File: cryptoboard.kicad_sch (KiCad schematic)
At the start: 29 parts, among them J1 USB_A, J2 BOOT, J3 SWD, J4 Conn_01x06, J5 Conn_01x06, SW1 SW_Push, U1 STM32F103C8Tx, U2 LM317_SOT-223-3.3V

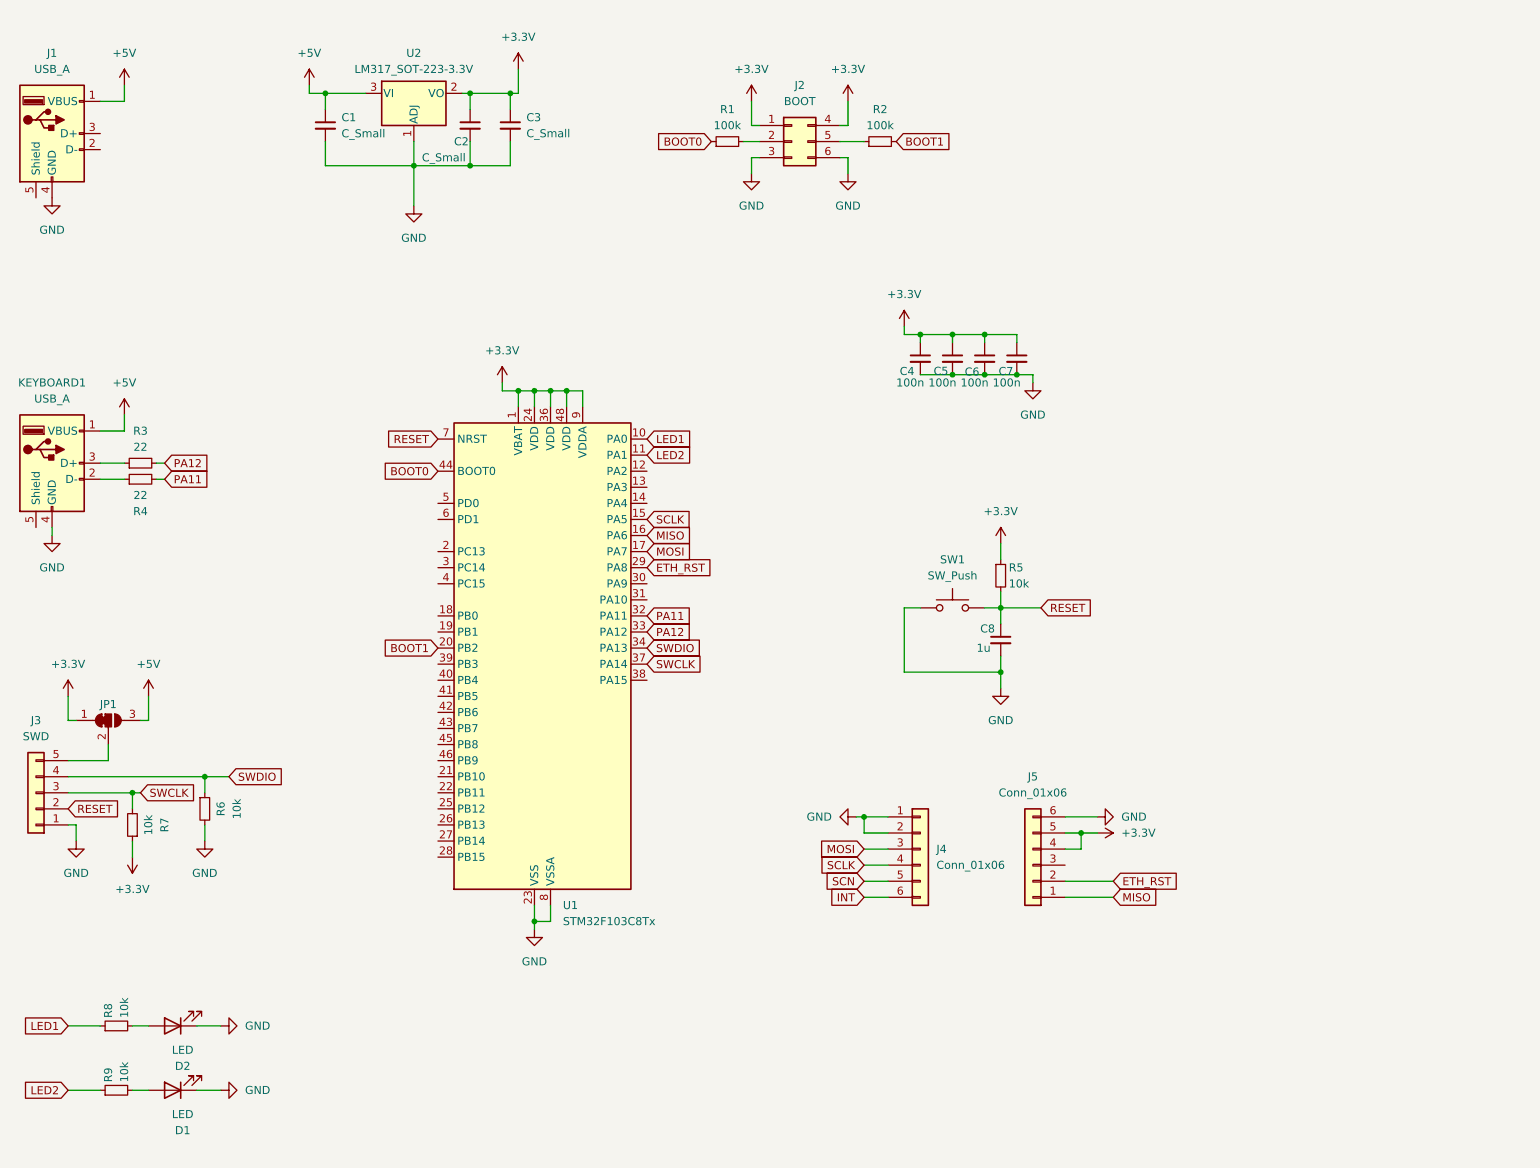
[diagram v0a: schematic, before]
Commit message: add i2c + usr
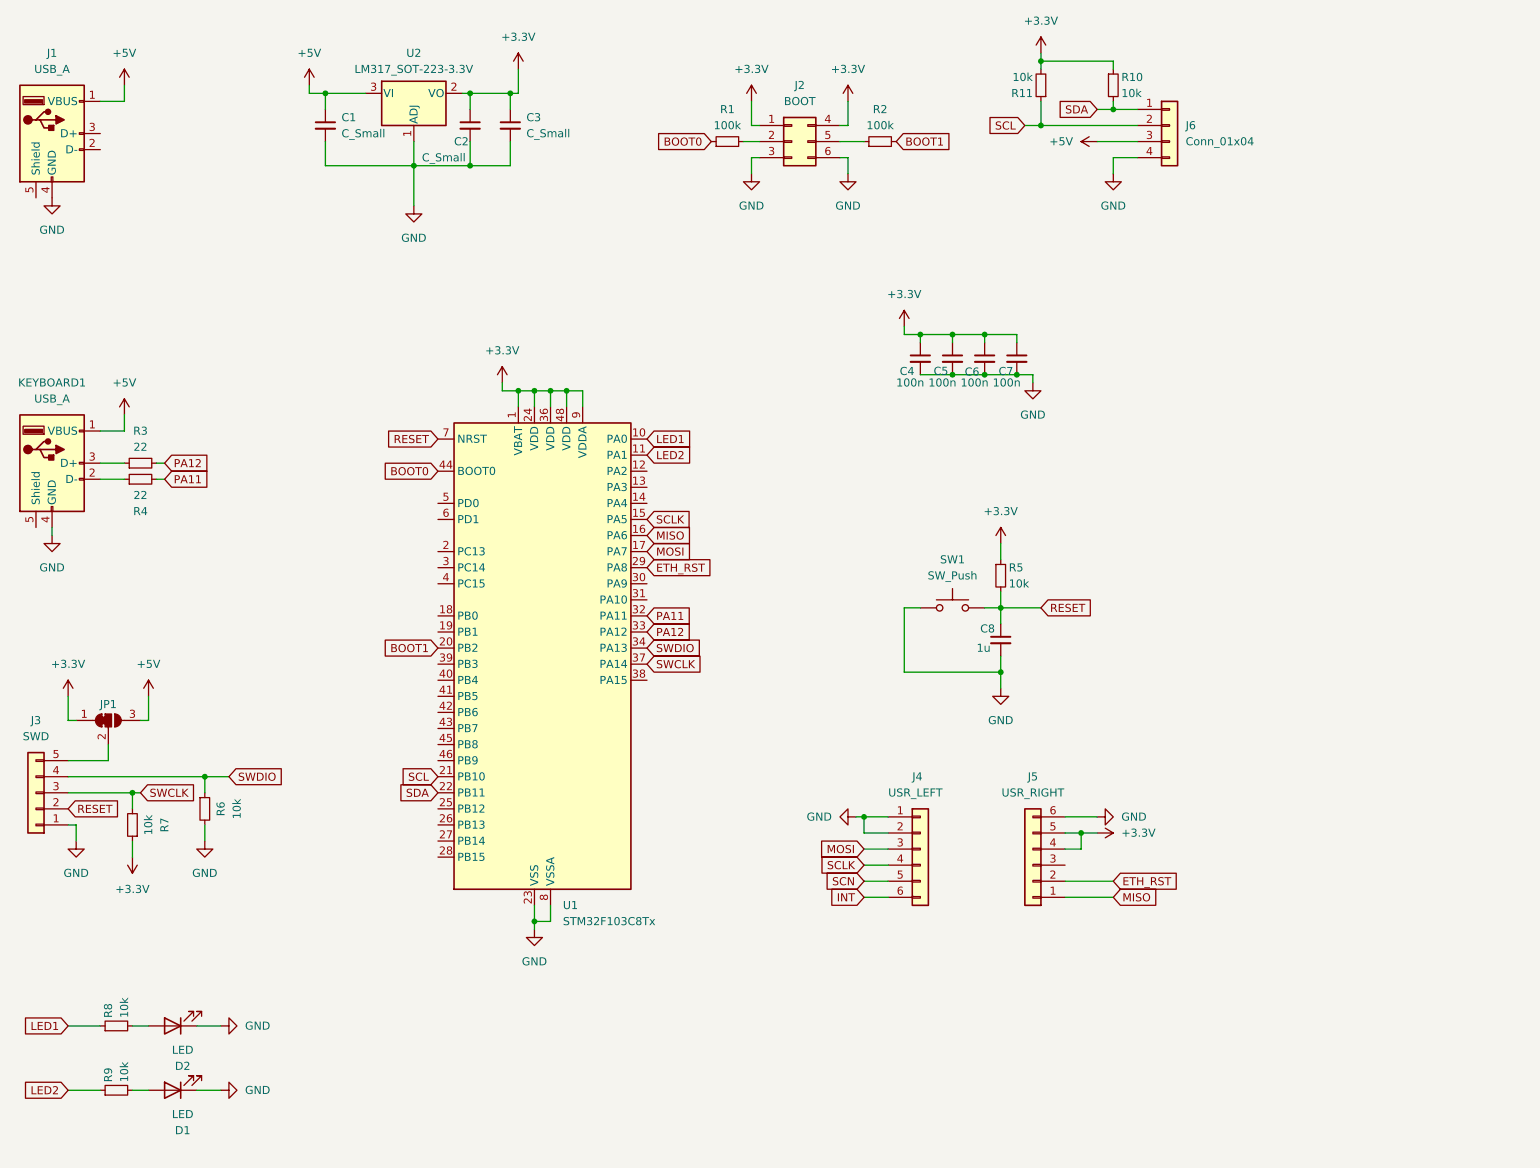
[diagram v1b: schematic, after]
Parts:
- added J6: Conn_01x04, Connector_PinHeader_2.54mm:PinHeader_1x04_P2.54mm_Vertical, symbol Connector_Generic:Conn_01x04
- added R10, R11: 10k, Resistor_SMD:R_0603_1608Metric, symbol Device:R_Small
- J4: value Conn_01x06 -> USR_LEFT; footprint (none) -> Connector_PinHeader_2.54mm:PinHeader_1x06_P2.54mm_Vertical
- J5: value Conn_01x06 -> USR_RIGHT; footprint (none) -> Connector_PinHeader_2.54mm:PinHeader_1x06_P2.54mm_Vertical
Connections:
- net +3.3V: now also R10.1, R11.2
- net +5V: now also J6.3 (Pin_3)
- net GND: now also J6.4 (Pin_4)
- net SCL: now reaches U1.21 (PB10)
- net SCL: now also J6.2 (Pin_2), R11.1
- net SDA: now reaches U1.22 (PB11)
- net SDA: now also J6.1 (Pin_1), R10.2

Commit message: add pcb
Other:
- moved on the sheet: R2
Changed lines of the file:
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@@
+    (stroke (width 0) (type default))
+  )
+  (wire (pts (xy 124.46 33.02) (xy 125.73 33.02))
     (stroke (width 0) (type default))
   )
@@
     (stroke (width 0) (type default))
   )
-  (wire (pts (xy 146.05 33.02) (xy 149.86 33.02))
+  (wire (pts (xy 146.05 33.02) (xy 148.59 33.02))
     (stroke (width 0) (type default))
   )
@@
   )
   (wire (pts (xy 64.77 33.02) (xy 64.77 36.83))
+    (stroke (width 0) (type default))
+  )
+  (wire (pts (xy 154.94 33.02) (xy 153.67 33.02))
     (stroke (width 0) (type default))
   )
@@
     )
   )
-  (global_label "BOOT0" (shape input) (at 125.73 33.02 180) (fields_autoplaced)
+  (global_label "BOOT0" (shape input) (at 124.46 33.02 180) (fields_autoplaced)
     (effects (font (size 1.27 1.27)) (justify right))
-    (property "Intersheetrefs" "${INTERSHEET_REFS}" (at 116.7161 33.02 0)
+    (property "Intersheetrefs" "${INTERSHEET_REFS}" (at 115.4461 33.02 0)
       (effects (font (size 1.27 1.27)) (justify right) hide)
     )
@@
     )
   )
-  (symbol (lib_id "Device:R_Small") (at 152.4 33.02 90) (unit 1)
-    (in_bom yes) (on_board yes) (dnp no) (fields_autoplaced)
-    (property "Reference" "R2" (at 152.4 27.94 90)
-      (effects (font (size 1.27 1.27)))
-    )
-    (property "Value" "100k" (at 152.4 30.48 90)
-      (effects (font (size 1.27 1.27)))
-    )
-    (property "Footprint" "Resistor_SMD:R_0603_1608Metric" (at 152.4 33.02 0)
-      (effects (font (size 1.27 1.27)) hide)
-    )
-    (property "Datasheet" "~" (at 152.4 33.02 0)
-      (effects (font (size 1.27 1.27)) hide)
-    )
+  (symbol (lib_id "Device:R_Small") (at 151.13 33.02 90) (unit 1)
+    (in_bom yes) (on_board yes) (dnp no) (fields_autoplaced)
+    (property "Reference" "R2" (at 151.13 27.94 90)
+      (effects (font (size 1.27 1.27)))
+    )
+    (property "Value" "100k" (at 151.13 30.48 90)
+      (effects (font (size 1.27 1.27)))
+    )
+    (property "Footprint" "Resistor_SMD:R_0603_1608Metric" (at 151.13 33.02 0)
+      (effects (font (size 1.27 1.27)) hide)
+    )
+    (property "Datasheet" "~" (at 151.13 33.02 0)
+      (effects (font (size 1.27 1.27)) hide)
+    )

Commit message: add wiring
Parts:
- J2: footprint Connector_PinHeader_2.54mm:PinHeader_2x03_P2.54mm_Vertical -> Library:PinHeader_2x03_P2.54mm_Vertical_new
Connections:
- net INT: now also U1.18 (PB0)
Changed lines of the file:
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@@
+    )
+  )
+  (global_label "INT" (shape input) (at 82.55 107.95 180) (fields_autoplaced)
+    (effects (font (size 1.27 1.27)) (justify right))
+    (property "Intersheetrefs" "${INTERSHEET_REFS}" (at 76.7413 107.95 0)
+      (effects (font (size 1.27 1.27)) (justify right) hide)
     )
   )
@@
       (effects (font (size 1.27 1.27)))
     )
-    (property "Footprint" "Connector_PinHeader_2.54mm:PinHeader_2x03_P2.54mm_Vertical" (at 138.43 33.02 0)
-      (effects (font (size 1.27 1.27)) hide)
-    )
+    (property "Footprint" "Library:PinHeader_2x03_P2.54mm_Vertical_new" (at 138.43 33.02 0)
+      (effects (font (size 1.27 1.27)) hide)
+    )

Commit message: add crystal
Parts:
- added C10, C9: 20p, Capacitor_SMD:C_0603_1608Metric, symbol Device:C_Small
- added R12: 1M, Resistor_SMD:R_0603_1608Metric, symbol Device:R_Small
- added Y1: Crystal, Crystal:Crystal_SMD_HC49-SD, symbol Device:Crystal
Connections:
- net GND: now also C10.2, C9.2
- net OSIN: now reaches U1.5 (PD0)
- net OSIN: now also C9.1, R12.1, Y1.2
- net OSOUT: now reaches U1.6 (PD1)
- net OSOUT: now also C10.1, R12.2, Y1.1

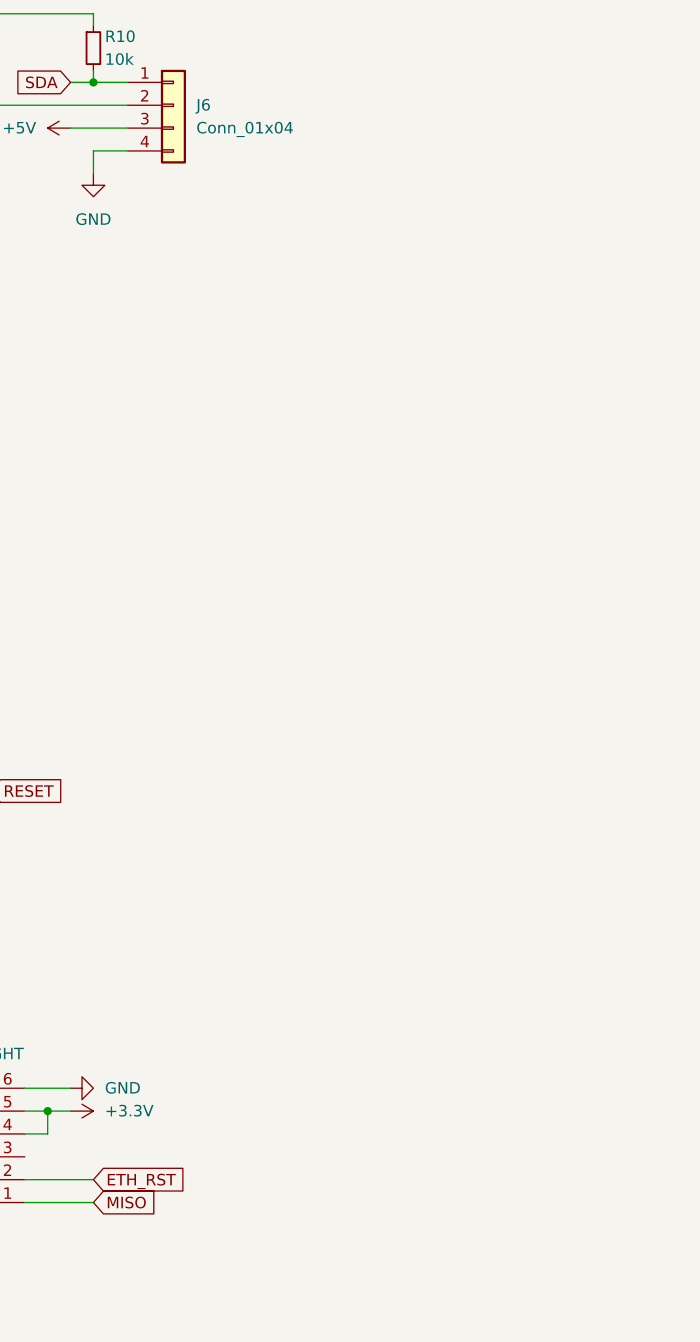
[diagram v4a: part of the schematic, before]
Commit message: stm32f103 to stm32f107
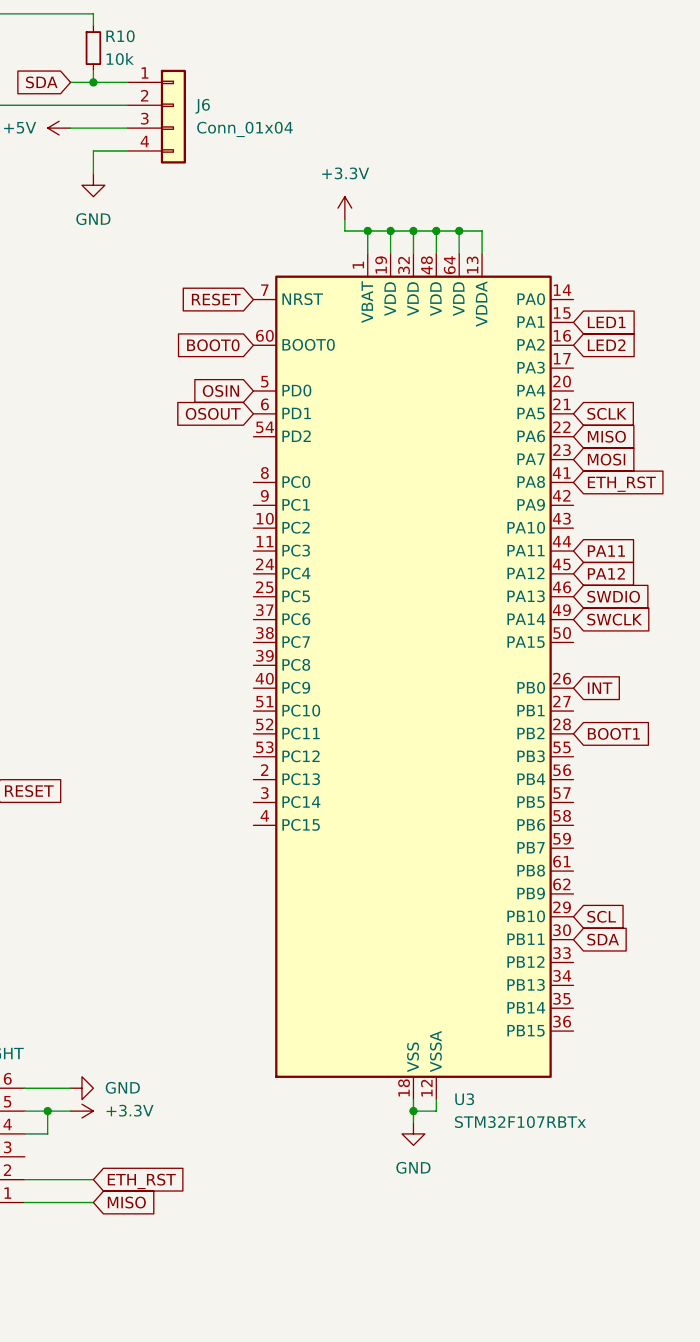
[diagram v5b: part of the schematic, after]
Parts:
- added U3: STM32F107RBTx, Package_QFP:LQFP-64_10x10mm_P0.5mm, symbol MCU_ST_STM32F1:STM32F107RBTx
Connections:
- net +3.3V: now also U3.1 (VBAT), U3.13 (VDDA), U3.19 (VDD), U3.32 (VDD), U3.48 (VDD), U3.64 (VDD)
- net BOOT0: now also U3.60 (BOOT0)
- net BOOT1: now also U3.28 (PB2)
- net ETH_RST: now also U3.41 (PA8)
- net GND: now also U3.12 (VSSA), U3.18 (VSS), U3.31 (VSS), U3.47 (VSS), U3.63 (VSS)
- net INT: now also U3.26 (PB0)
- net LED1: now also U3.15 (PA1)
- net LED2: now also U3.16 (PA2)
- net MISO: now also U3.22 (PA6)
- net MOSI: now also U3.23 (PA7)
- net OSIN: now also U3.5 (PD0)
- net OSOUT: now also U3.6 (PD1)
- net PA11: now also U3.44 (PA11)
- net PA12: now also U3.45 (PA12)
- net RESET: now also U3.7 (NRST)
- net SCL: now also U3.29 (PB10)
- net SCLK: now also U3.21 (PA5)
- net SDA: now also U3.30 (PB11)
- net SWCLK: now also U3.49 (PA14)
- net SWDIO: now also U3.46 (PA13)
